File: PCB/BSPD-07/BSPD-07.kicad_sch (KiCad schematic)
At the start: 18 parts

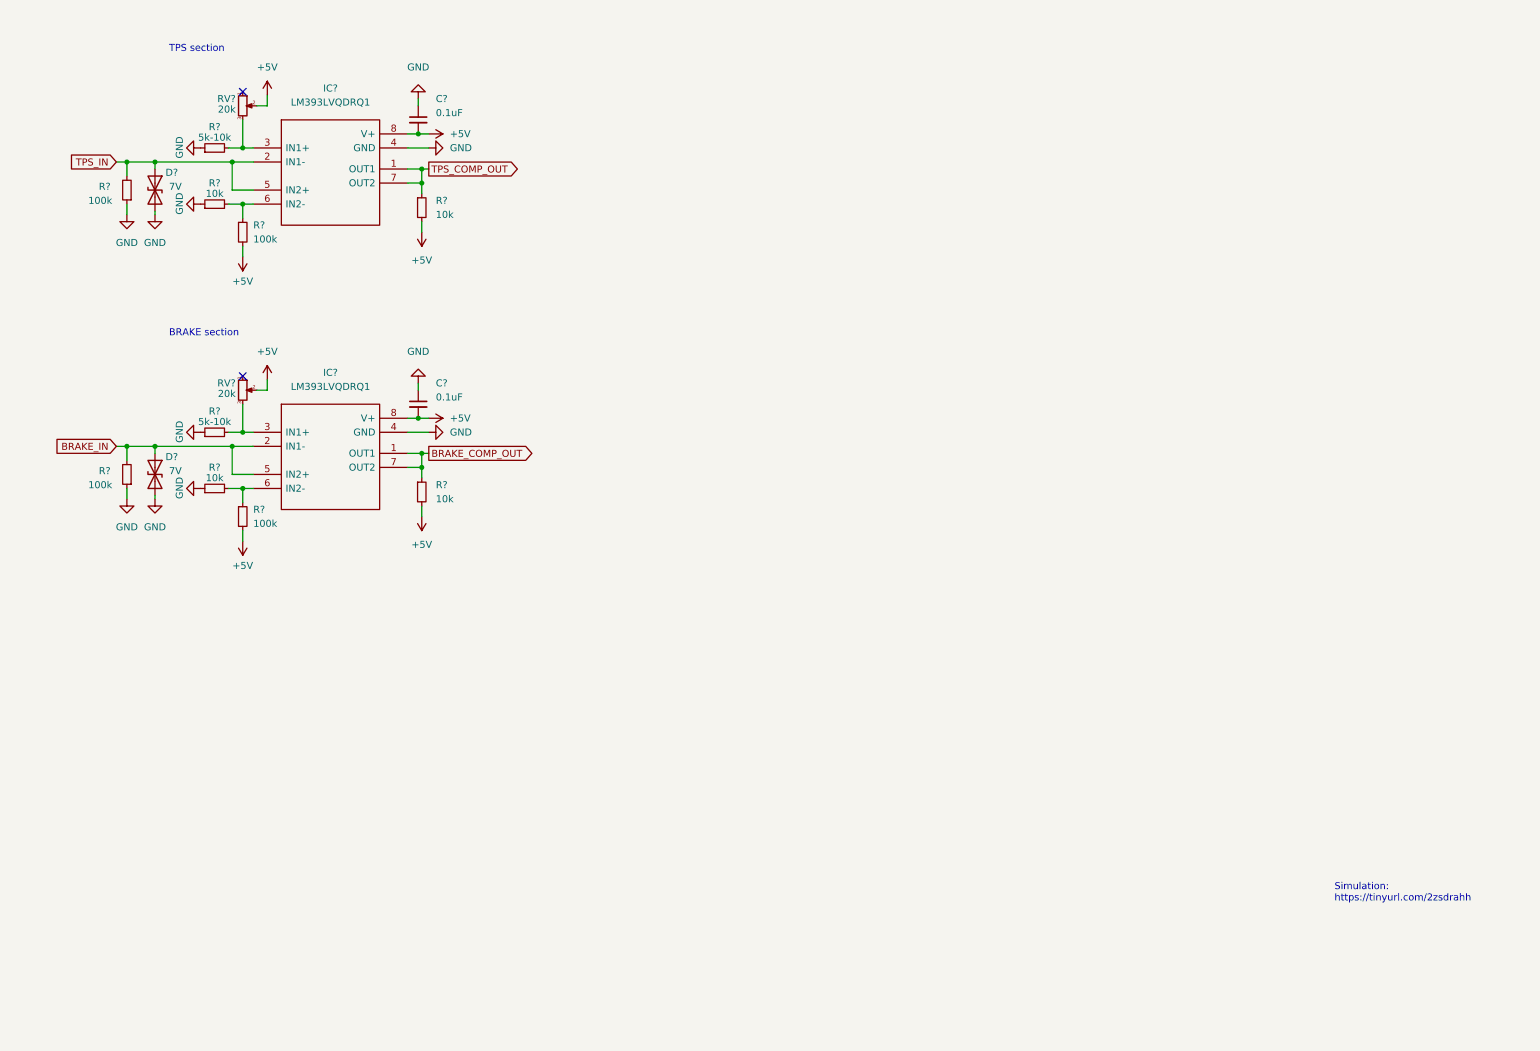
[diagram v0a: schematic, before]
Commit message: Added connector and delay section
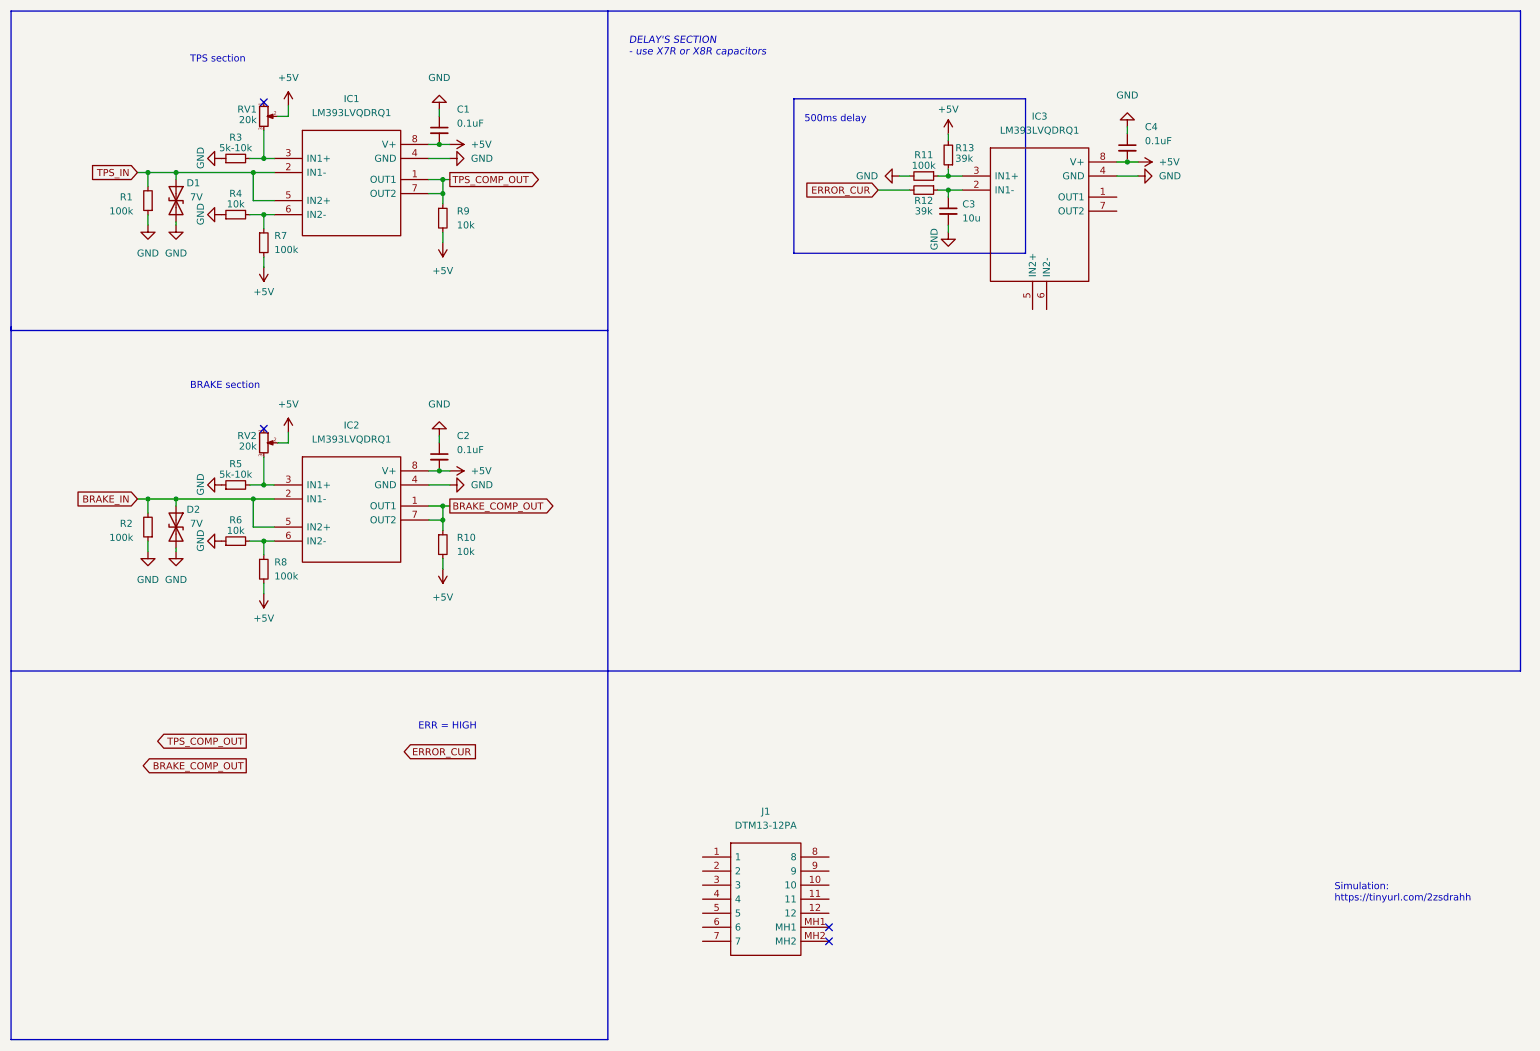
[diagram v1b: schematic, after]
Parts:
- added C3: 10u, symbol Device:C_Small
- added C4: 0.1uF, symbol Device:C_Small
- added IC3: LM393LVQDRQ1, PDM_Additional:SOIC127P600X175-8N, symbol BSPD-07:LM393LVQDRQ1
- added J1: DTM13-12PA, BSPD_07:DTM1312PA, symbol BSPD-07:DTM13-12PA
- added R11: 100k, Resistor_SMD:R_0402_1005Metric, symbol Device:R_Small
- added R12, R13: 39k, Resistor_SMD:R_0402_1005Metric, symbol Device:R_Small
- IC1, IC2: renamed from IC?; footprint SOIC127P600X175-8N -> PDM_Additional:SOIC127P600X175-8N
- R1, R10, R2, R3, R4, R5, R6, R7, R8, R9: renamed from R?; footprint (none) -> Resistor_SMD:R_0402_1005Metric
- gave numbers to parts that had none: 6
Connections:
- net +5V: now also C4.2, IC3.8 (V+), R13.2
- net GND: now also C3.2, C4.1, IC3.4 (GND), R11.2
- new net: IC3.3 (IN1+), R11.1, R13.1
- new net: C3.1, IC3.2 (IN1-), R12.1
- new net ERROR_CUR: R12.2
- no-connect marks 2 -> 4
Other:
- note added: "500ms delay"
- note added: "DELAY'S SECTION - use X7R or X8R capacitors"
- note added: "ERR = HIGH"
- moved on the sheet: C1, C2, D1, D2, IC1, IC2, R1, R10, R2, R3, R4, R5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

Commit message: New revision with LDO40L
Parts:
- added C5: 10uF, Capacitor_SMD:C_0805_2012Metric, symbol Device:C_Small
- added C6: 1uF, Capacitor_SMD:C_0805_2012Metric, symbol Device:C_Small
- added C7: 4.7uF, Capacitor_SMD:C_0805_2012Metric, symbol Device:C_Small
- added IC4: LDO40LPU50RY, symbol BSPD-07:LDO40LPU50RY
- added Q1: RSQ025P03HZGTR, symbol BSPD-07:RSQ025P03HZGTR
- added R14: 5, symbol Device:R_Small
- added R15: 560k, symbol Device:R_Small
- C1, C2, C4: footprint (none) -> Capacitor_SMD:C_0402_1005Metric
- C3: footprint (none) -> Capacitor_SMD:C_0805_2012Metric
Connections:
- net +5V: now also C5.1, C7.1, IC4.4 (VOUT), IC4.5 (VSENSE), Q1.4 (SOURCE)
- net GND: now also J1.MH1, C6.2, C7.2, IC4.1 (GND_1), IC4.7 (GND_2), R15.2
- net BRAKE_TRIG: now reaches IC2.3 (IN1+), R5.2, RV2.3
- net BRAKE_TRIG: now also J1.8
- net at IC3.1 (OUT1): now also Q1.3 (GATE)
- net at IC3.6 (IN2-): now also C5.2, R14.2, R15.1
- net SAFETY_IN: now reaches J1.5
- net SAFETY_OUT: now reaches J1.6
- net TPS_TRIG: now reaches J1.7
- net TPS_TRIG: now also IC1.3 (IN1+), R3.2, RV1.3
- net +12V: now reaches J1.MH2
- net +12V: now also C6.1, IC4.2 (EN), IC4.3 (VIN)
- net ERROR_CUR renamed ERR_CURRENT
- new net: Q1.1 (DRAIN_1), Q1.2 (DRAIN_2), Q1.5 (DRAIN_3), Q1.6 (DRAIN_4), R14.1
- no-connect marks 4 -> 5
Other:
- note added: "Discharging capacitor when implausibility occurs"
- note added: "LDO"
- note added: "X7R capacitors close to pins"
- moved on the sheet: J1, R3, R5, RV1, RV2

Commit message: Almost finished schematics
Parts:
- added IC5: 74LVC1G02GW-Q100H, SOT65P212X110-5N, symbol BSPD-07:74LVC1G02GW-Q100H
- added TP?: TPS, symbol Connector:TestPoint_Small
- added TP?: BRK, symbol Connector:TestPoint_Small
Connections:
- net +5V: now also IC5.5 (VCC)
- net BRAKE_COMP_OUT: now also IC5.2 (A), TP?.1
- net ERR_CURRENT: now also IC5.4 (Y)
- net GND: now also IC5.3 (GND)
- net TPS_COMP_OUT: now also IC5.1 (B), TP?.1
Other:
- note added: "BRAKE WINDOW DETECTOR 0.45V to TRIG_H"
- note added: "NOR"
- note added: "TPS WINDOW DETECTOR 0.45V to TRIG_H"
- note removed: "BRAKE section"
- note removed: "TPS section"
- moved on the sheet: C1, D1, IC1, R1, R3, R4, R7, R9, RV1

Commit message: Finished schematics
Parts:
- added C8: 100u, symbol Device:C_Small
- added JP1: Jumper_2_Open, Connector_PinHeader_2.54mm:PinHeader_1x02_P2.54mm_Vertical, symbol Jumper:Jumper_2_Open
- added Q2, Q?: RJU002N06FRAT106, BSPD_07:SOT65P210X100-3N, symbol BSPD-07:RJU002N06FRAT106
- added R16, R18: 100, symbol Device:R_Small
- added R17, R19: 10k, symbol Device:R_Small
- added R20: 560k, symbol Device:R_Small
- added R21: 2-4, symbol Device:R_Small
- added R?: 1k, symbol Device:R_Small
- added U2: TLP175A / COMUS AB38-Q, Package_SO:MFSOP6-4_4.4x3.6mm_P1.27mm, symbol Relay_SolidState:TLP175A
- IC1, IC2, IC3: footprint PDM_Additional:SOIC127P600X175-8N -> BSPD_07:SOIC127P600X175-8N
- IC4: footprint (none) -> BSPD_07:SON95P300X300X90-7N-D
- IC5: footprint SOT65P212X110-5N -> BSPD_07:SOT65P212X110-5N
- Q1: footprint (none) -> BSPD_07:SOT95P280X100-6N
- R14, R15: footprint (none) -> Resistor_SMD:R_0402_1005Metric
- R7, R8: value 100k -> 200k
- RV1, RV2: footprint (none) -> BSPD_07:POT-3296X1223LF
- gave numbers to parts that had none: 2
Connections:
- net +12V: now also J1.1; no longer J1.MH2
- net +5V: now also C8.1, R17.2, R19.2, R?.2
- net BRAKE_IN: now also J1.11
- net GND: now also J1.2, Q?.2, R20.2, R21.1; no longer J1.MH1
- net SAFETY_IN: now also JP1.1 (A), U2.6
- net SAFETY_OUT: now also JP1.2 (B), U2.4
- net TPS_IN: now also J1.12
- net at IC3.1 (OUT1): now also R16.1; no longer Q1.3 (GATE)
- net at C5.2, IC3.6 (IN2-), R14.2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: now also Q2.3
- net at IC3.7 (OUT2): now also R18.1, R19.1
- new net: R?.1, U2.1
- new net: Q1.3 (GATE), R16.2, R17.1
- new net: Q?.3, U2.3
- new net: Q2.2, R21.2
- new net: C8.2, Q2.1, R20.1
- new net ERR_FINAL: Q?.1, R18.2
- no-connect marks 5 -> 10
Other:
- note added: "500MS DELAY"
- note added: "BRAKE WINDOW DETECTOR 0.24V to TRIG_H"
- note added: "BSPD for PGR-07 (2023)"
- note added: "ERR = LOW"
- note added: "HEADER"
- note added: "INFO"
- note added: "PRECHARGE CIRCUIT"
- note added: "SAFETY SWITCH"
- note added: "TPS WINDOW DETECTOR 0.24V to TRIG_H"
- note added: "Test purposes only ;)"
- note removed: "500ms delay"
- note removed: "BRAKE WINDOW DETECTOR 0.45V to TRIG_H"
- note removed: "TPS WINDOW DETECTOR 0.45V to TRIG_H"
- moved on the sheet: C3, C4, C5, IC3, IC5, J1, Q1, R11, R12, R13, R14, R15

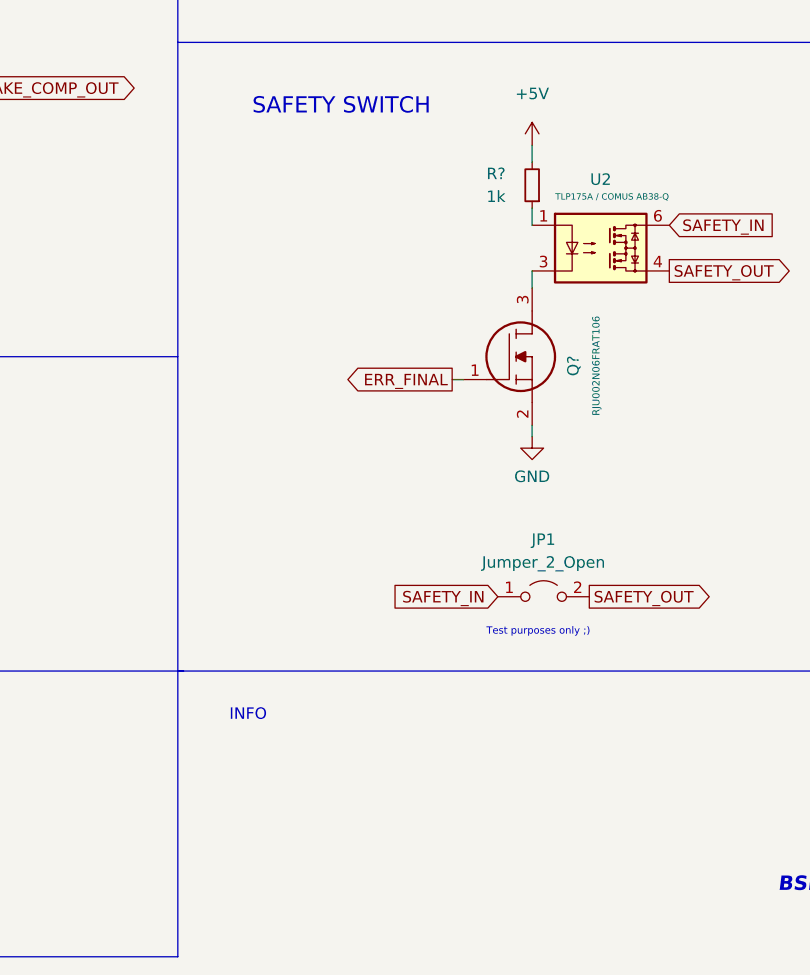
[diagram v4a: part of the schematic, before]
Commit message: Added info led
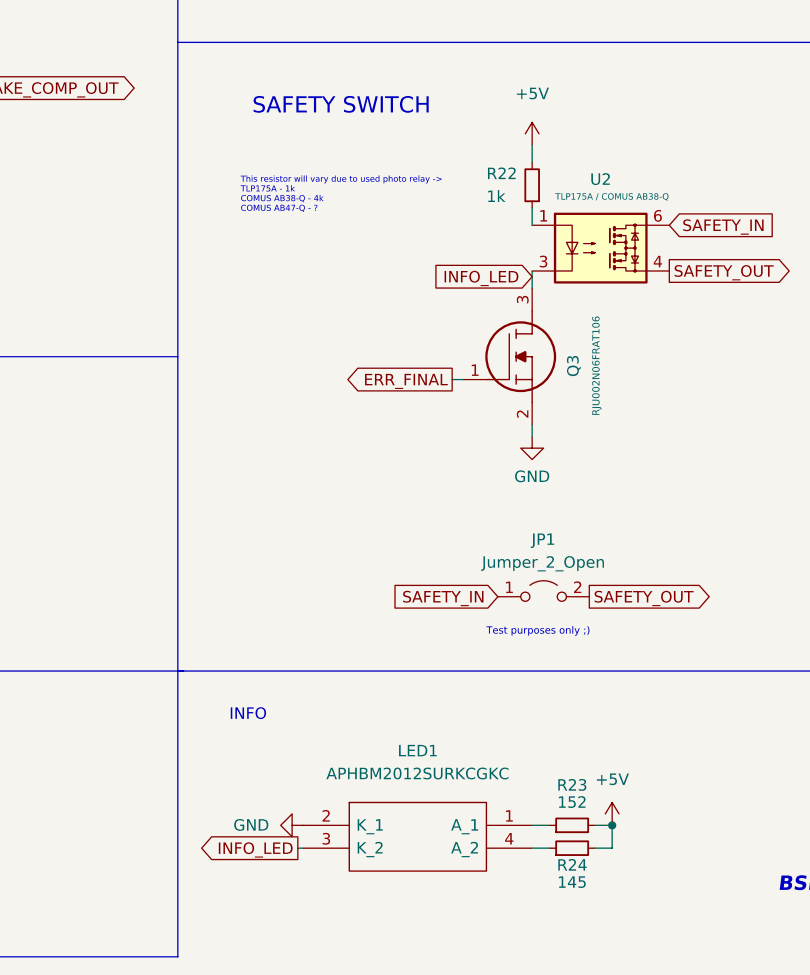
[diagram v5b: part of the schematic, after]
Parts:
- added LED1: APHBM2012SURKCGKC, APHBM2012SURKCGKC, symbol BSPD-07:APHBM2012SURKCGKC
- added R23: 152, symbol Device:R_Small
- added R24: 145, symbol Device:R_Small
- gave numbers to parts that had none: 2
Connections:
- net +5V: now also R23.2, R24.2
- net GND: now also LED1.2 (K_1)
- net INFO_LED: now reaches Q3.3, U2.3
- net INFO_LED: now also LED1.3 (K_2)
- new net: LED1.4 (A_2), R24.1
- new net: LED1.1 (A_1), R23.1
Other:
- note added: "This resistor will vary due to used photo relay -> TLP175A - 1k COMUS AB38-Q - 4k COMUS AB47-Q - ?"
